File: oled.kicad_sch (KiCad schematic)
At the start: 10 parts

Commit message: wip
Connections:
- net VBUS is gone; now on net +3V3: R26.1
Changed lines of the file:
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@@
-    )
-  )
-  (symbol (lib_id "power:VBUS") (at 100.33 93.98 0) (unit 1)
-    (in_bom yes) (on_board yes) (dnp no) (fields_autoplaced)
-    (property "Reference" "#PWR02" (at 100.33 97.79 0)
-      (effects (font (size 1.27 1.27)) hide)
-    )
-    (property "Value" "VBUS" (at 100.33 90.4781 0)
-      (effects (font (size 1.27 1.27)))
-    )
-    (property "Footprint" "" (at 100.33 93.98 0)
-      (effects (font (size 1.27 1.27)) hide)
-    )
-    (property "Datasheet" "" (at 100.33 93.98 0)
-      (effects (font (size 1.27 1.27)) hide)
-    )
-    (pin "1")
-    (instances
-      (project "oled-nametag"
-        (path "/c0b8a503-1da4-4e1a-941c-dddf39a5c519"
-          (reference "#PWR02") (unit 1)
-        )
-        (path "/c0b8a503-1da4-4e1a-941c-dddf39a5c519/4a47d447-b016-4135-8945-1a7aa01f0126"
-          (reference "#PWR03") (unit 1)
-        )
-      )
     )
   )
@@
         )
       )
+    )
+  )
+  (symbol (lib_id "power:+3V3") (at 100.33 93.98 0) (unit 1)
+    (in_bom yes) (on_board yes) (dnp no) (fields_autoplaced)
+    (property "Reference" "#PWR03" (at 100.33 97.79 0)
+      (effects (font (size 1.27 1.27)) hide)
+    )
+    (property "Value" "+3V3" (at 100.33 90.4781 0)
+      (effects (font (size 1.27 1.27)))
+    )
+    (property "Footprint" "" (at 100.33 93.98 0)
+      (effects (font (size 1.27 1.27)) hide)
+    )
+    (property "Datasheet" "" (at 100.33 93.98 0)
+      (effects (font (size 1.27 1.27)) hide)
+    )
+    (pin "1")
+    (instances
+      (project "oled-nametag"
+        (path "/c0b8a503-1da4-4e1a-941c-dddf39a5c519/4a47d447-b016-4135-8945-1a7aa01f0126"
+          (reference "#PWR03") (unit 1)
+        )
+      )

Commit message: Finish first layout revision
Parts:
- added C33: 100nF, Capacitor_SMD:C_0402_1005Metric, symbol Device:C_Small
- R26: value 5.1k -> 100R; LCSC C25905 -> C25076
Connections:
- net GND: now also U1.ML (MP), C33.1
- net OLED_RST: now also C33.2
- new net GND1: U1.MR (MP)
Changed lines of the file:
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@@
 (kicad_sch (version 20230121) (generator eeschema)
   (paper "A4")
+  (junction (at 95.25 114.3) (diameter 0) (color 0 0 0 0)
+  )
   (junction (at 127 143.51) (diameter 0) (color 0 0 0 0)
   )
@@
   (junction (at 109.22 134.62) (diameter 0) (color 0 0 0 0)
   )
+  (junction (at 91.44 104.14) (diameter 0) (color 0 0 0 0)
+  )
   (junction (at 109.22 127) (diameter 0) (color 0 0 0 0)
   )
@@
     (stroke (width 0) (type default))
   )
+  (wire (pts (xy 95.25 99.06) (xy 95.25 114.3))
+    (stroke (width 0) (type default))
+  )
   (wire (pts (xy 144.78 115.57) (xy 144.78 116.84))
     (stroke (width 0) (type default))
   )
+  (wire (pts (xy 132.08 143.51) (xy 133.35 143.51))
+    (stroke (width 0) (type default))
+  )
+  (wire (pts (xy 137.16 143.51) (xy 135.89 143.51))
+    (stroke (width 0) (type default))
+  )
   (wire (pts (xy 110.49 88.9) (xy 110.49 80.01))
     (stroke (width 0) (type default))
@@
     (stroke (width 0) (type default))
   )
+  (wire (pts (xy 91.44 104.14) (xy 91.44 105.41))
+    (stroke (width 0) (type default))
+  )
   (wire (pts (xy 143.51 109.22) (xy 144.78 109.22))
     (stroke (width 0) (type default))
@@
     (stroke (width 0) (type default))
   )
+  (wire (pts (xy 135.89 142.24) (xy 135.89 143.51))
+    (stroke (width 0) (type default))
+  )
   (wire (pts (xy 129.54 87.63) (xy 132.08 87.63))
     (stroke (width 0) (type default))
@@
     (stroke (width 0) (type default))
   )
-  (wire (pts (xy 95.25 104.14) (xy 95.25 99.06))
-    (stroke (width 0) (type default))
-  )
-  (wire (pts (xy 109.22 104.14) (xy 110.49 104.14))
+  (wire (pts (xy 90.17 104.14) (xy 91.44 104.14))
     (stroke (width 0) (type default))
   )
@@
     (stroke (width 0) (type default))
   )
+  (wire (pts (xy 91.44 110.49) (xy 91.44 111.76))
+    (stroke (width 0) (type default))
+  )
+  (wire (pts (xy 132.08 144.78) (xy 132.08 143.51))
+    (stroke (width 0) (type default))
+  )
   (wire (pts (xy 109.22 132.08) (xy 109.22 129.54))
     (stroke (width 0) (type default))
   )
+  (wire (pts (xy 133.35 142.24) (xy 133.35 143.51))
+    (stroke (width 0) (type default))
+  )
   (wire (pts (xy 109.22 129.54) (xy 109.22 127))
     (stroke (width 0) (type default))
   )
+  (wire (pts (xy 91.44 104.14) (xy 110.49 104.14))
+    (stroke (width 0) (type default))
+  )
   (wire (pts (xy 172.72 96.52) (xy 143.51 96.52))
     (stroke (width 0) (type default))
@@
   )
   (wire (pts (xy 144.78 109.22) (xy 144.78 110.49))
+    (stroke (width 0) (type default))
+  )
+  (wire (pts (xy 137.16 144.78) (xy 137.16 143.51))
     (stroke (width 0) (type default))
   )
@@
     (effects (font (size 1.27 1.27)) (justify left))
   )
-  (hierarchical_label "OLED_RST" (shape input) (at 109.22 104.14 180) (fields_autoplaced)
+  (hierarchical_label "OLED_RST" (shape input) (at 90.17 104.14 180) (fields_autoplaced)
     (effects (font (size 1.27 1.27)) (justify right))
   )
@@
   )
   (symbol (lib_id "OLED:OLED_256x64") (at 127 116.84 0) (unit 1)
-    (in_bom yes) (on_board yes) (dnp no) (fields_autoplaced)
-    (property "Reference" "U1" (at 130.2259 141.2955 0)
+    (in_bom yes) (on_board yes) (dnp no)
+    (property "Reference" "U1" (at 118.11 92.71 0)
       (effects (font (size 1.27 1.27)) (justify left))
     )
@@
     (pin "29")
     (pin "30")
+    (pin "ML")
+    (pin "MR")
     (instances
       (project "oled-nametag"
@@
         (path "/c0b8a503-1da4-4e1a-941c-dddf39a5c519/4a47d447-b016-4135-8945-1a7aa01f0126"
           (reference "U1") (unit 1)
+        )
+      )
+    )
+  )
+  (symbol (lib_id "power:GND") (at 91.44 111.76 0) (unit 1)
+    (in_bom yes) (on_board yes) (dnp no) (fields_autoplaced)
+    (property "Reference" "#PWR01" (at 91.44 118.11 0)
+      (effects (font (size 1.27 1.27)) hide)
+    )
+    (property "Value" "GND" (at 91.44 115.8955 0)
+      (effects (font (size 1.27 1.27)))
+    )
+    (property "Footprint" "" (at 91.44 111.76 0)
+      (effects (font (size 1.27 1.27)) hide)
+    )
+    (property "Datasheet" "" (at 91.44 111.76 0)
+      (effects (font (size 1.27 1.27)) hide)
+    )
+    (pin "1")
+    (instances
+      (project "oled-nametag"
+        (path "/c0b8a503-1da4-4e1a-941c-dddf39a5c519/4a47d447-b016-4135-8945-1a7aa01f0126"
+          (reference "#PWR01") (unit 1)
         )
       )
@@
     )
   )
+  (symbol (lib_id "power:GND1") (at 137.16 144.78 0) (unit 1)
+    (in_bom yes) (on_board yes) (dnp no) (fields_autoplaced)
+    (property "Reference" "#PWR082" (at 137.16 151.13 0)
+      (effects (font (size 1.27 1.27)) hide)
+    )
+    (property "Value" "GND1" (at 137.16 148.9155 0)
+      (effects (font (size 1.27 1.27)))
+    )
+    (property "Footprint" "" (at 137.16 144.78 0)
+      (effects (font (size 1.27 1.27)) hide)
+    )
+    (property "Datasheet" "" (at 137.16 144.78 0)
+      (effects (font (size 1.27 1.27)) hide)
+    )
+    (pin "1")
+    (instances
+      (project "oled-nametag"
+        (path "/c0b8a503-1da4-4e1a-941c-dddf39a5c519/4a47d447-b016-4135-8945-1a7aa01f0126"
+          (reference "#PWR082") (unit 1)
+        )
+      )
+    )
+  )
   (symbol (lib_id "power:GND") (at 144.78 116.84 0) (unit 1)
     (in_bom yes) (on_board yes) (dnp no) (fields_autoplaced)
@@
       (effects (font (size 1.27 1.27)))
     )
-    (property "Value" "5.1k" (at 107.95 93.98 90)
+    (property "Value" "100R" (at 107.95 93.98 90)
       (effects (font (size 1.27 1.27)))
     )
@@
       (effects (font (size 1.27 1.27)) hide)
     )
-    (property "LCSC" "C25905" (at 106.68 96.52 0)
+    (property "LCSC" "C25076" (at 106.68 96.52 0)
       (effects (font (size 1.27 1.27)) hide)
     )
@@
         (path "/c0b8a503-1da4-4e1a-941c-dddf39a5c519/4a47d447-b016-4135-8945-1a7aa01f0126"
           (reference "#PWR017") (unit 1)
-        )
-      )
-    )
-  )
-  (symbol (lib_id "power:GND") (at 95.25 104.14 0) (unit 1)
-    (in_bom yes) (on_board yes) (dnp no) (fields_autoplaced)
-    (property "Reference" "#PWR01" (at 95.25 110.49 0)
-      (effects (font (size 1.27 1.27)) hide)
-    )
-    (property "Value" "GND" (at 95.25 108.2755 0)
-      (effects (font (size 1.27 1.27)))
-    )
-    (property "Footprint" "" (at 95.25 104.14 0)
-      (effects (font (size 1.27 1.27)) hide)
-    )
-    (property "Datasheet" "" (at 95.25 104.14 0)
-      (effects (font (size 1.27 1.27)) hide)
-    )
-    (pin "1")
-    (instances
-      (project "oled-nametag"
-        (path "/c0b8a503-1da4-4e1a-941c-dddf39a5c519"
-          (reference "#PWR01") (unit 1)
-        )
-        (path "/c0b8a503-1da4-4e1a-941c-dddf39a5c519/4a47d447-b016-4135-8945-1a7aa01f0126"
-          (reference "#PWR01") (unit 1)
         )
       )
@@
         )
       )
+    )
+  )
+  (symbol (lib_id "power:GND") (at 132.08 144.78 0) (unit 1)
+    (in_bom yes) (on_board yes) (dnp no) (fields_autoplaced)
+    (property "Reference" "#PWR014" (at 132.08 151.13 0)
+      (effects (font (size 1.27 1.27)) hide)
+    )
+    (property "Value" "GND" (at 132.08 148.9155 0)
+      (effects (font (size 1.27 1.27)))
+    )
+    (property "Footprint" "" (at 132.08 144.78 0)
+      (effects (font (size 1.27 1.27)) hide)
+    )
+    (property "Datasheet" "" (at 132.08 144.78 0)
+      (effects (font (size 1.27 1.27)) hide)
+    )
+    (pin "1")
+    (instances
+      (project "oled-nametag"
+        (path "/c0b8a503-1da4-4e1a-941c-dddf39a5c519"
+          (reference "#PWR014") (unit 1)
+        )
+        (path "/c0b8a503-1da4-4e1a-941c-dddf39a5c519/4a47d447-b016-4135-8945-1a7aa01f0126"
+          (reference "#PWR081") (unit 1)
+        )
+      )
+    )
+  )
+  (symbol (lib_id "Device:C_Small") (at 91.44 107.95 0) (mirror x) (unit 1)
+    (in_bom yes) (on_board yes) (dnp no)
+    (property "Reference" "C33" (at 87.63 109.22 0)
+      (effects (font (size 1.27 1.27)))
+    )
+    (property "Value" "100nF" (at 86.36 106.68 0)
+      (effects (font (size 1.27 1.27)))
+    )
+    (property "Footprint" "Capacitor_SMD:C_0402_1005Metric" (at 91.44 107.95 0)
+      (effects (font (size 1.27 1.27)) hide)
+    )
+    (property "Datasheet" "~" (at 91.44 107.95 0)
+      (effects (font (size 1.27 1.27)) hide)
+    )
+    (property "LCSC" "C1525" (at 91.44 107.95 90)
+      (effects (font (size 1.27 1.27)) hide)
+    )
+    (pin "1")
+    (pin "2")
+    (instances
+      (project "rgb-led-nametag-48x16"
+        (path "/751d823e-1d7b-4501-9658-d06d459b0e16"
+          (reference "C33") (unit 1)
+        )
+      )
+      (project "oled-nametag"
+        (path "/c0b8a503-1da4-4e1a-941c-dddf39a5c519"
+          (reference "C16") (unit 1)
+        )
+        (path "/c0b8a503-1da4-4e1a-941c-dddf39a5c519/2d7ad3ad-5e88-44f5-86dc-1521acbc3a27"
+          (reference "C17") (unit 1)
+        )
+        (path "/c0b8a503-1da4-4e1a-941c-dddf39a5c519/4a47d447-b016-4135-8945-1a7aa01f0126"
+          (reference "C39") (unit 1)
+        )
+      )

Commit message: Start rev1.1
Fixed bugs:
 - Swapped D+ and D-
 - Insufficient pull-down strength on VBUS
 - Default OLED to 4-wire SPI
 - Swap VBUS detect divider from 2/3 to 1/3
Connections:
- net +3V3: no longer R26.1
- net GND: now also R26.1
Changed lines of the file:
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@@
   (junction (at 124.46 88.9) (diameter 0) (color 0 0 0 0)
   )
+  (junction (at 95.25 99.06) (diameter 0) (color 0 0 0 0)
+  )
   (junction (at 109.22 134.62) (diameter 0) (color 0 0 0 0)
   )
@@
     (stroke (width 0) (type default))
   )
+  (wire (pts (xy 95.25 96.52) (xy 104.14 96.52))
+    (stroke (width 0) (type default))
+  )
   (wire (pts (xy 109.22 109.22) (xy 110.49 109.22))
     (stroke (width 0) (type default))
@@
     (stroke (width 0) (type default))
   )
-  (wire (pts (xy 100.33 96.52) (xy 104.14 96.52))
-    (stroke (width 0) (type default))
-  )
   (wire (pts (xy 109.22 139.7) (xy 109.22 137.16))
     (stroke (width 0) (type default))
@@
     (stroke (width 0) (type default))
   )
-  (wire (pts (xy 100.33 93.98) (xy 100.33 96.52))
-    (stroke (width 0) (type default))
-  )
   (wire (pts (xy 109.22 129.54) (xy 110.49 129.54))
     (stroke (width 0) (type default))
@@
   )
   (wire (pts (xy 129.54 78.74) (xy 129.54 87.63))
+    (stroke (width 0) (type default))
+  )
+  (wire (pts (xy 95.25 96.52) (xy 95.25 99.06))
     (stroke (width 0) (type default))
   )
@@
         )
       )
-    )
-  )
-  (symbol (lib_id "power:+3V3") (at 100.33 93.98 0) (unit 1)
-    (in_bom yes) (on_board yes) (dnp no) (fields_autoplaced)
-    (property "Reference" "#PWR03" (at 100.33 97.79 0)
-      (effects (font (size 1.27 1.27)) hide)
-    )
-    (property "Value" "+3V3" (at 100.33 90.4781 0)
-      (effects (font (size 1.27 1.27)))
-    )
-    (property "Footprint" "" (at 100.33 93.98 0)
-      (effects (font (size 1.27 1.27)) hide)
-    )
-    (property "Datasheet" "" (at 100.33 93.98 0)
-      (effects (font (size 1.27 1.27)) hide)
-    )
-    (pin "1")
-    (instances
-      (project "oled-nametag"
-        (path "/c0b8a503-1da4-4e1a-941c-dddf39a5c519/4a47d447-b016-4135-8945-1a7aa01f0126"
-          (reference "#PWR03") (unit 1)
-        )
-      )

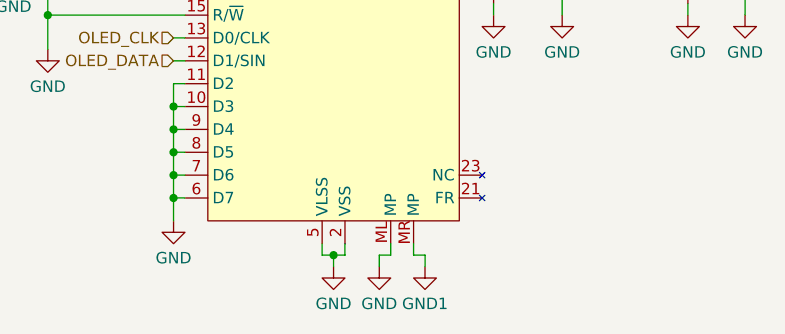
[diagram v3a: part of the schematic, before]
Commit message: Do rough component placement
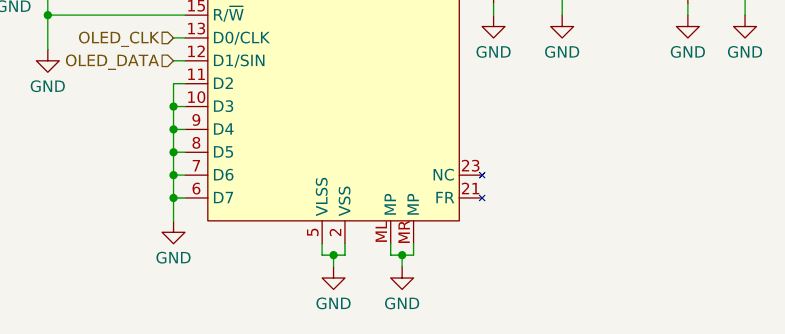
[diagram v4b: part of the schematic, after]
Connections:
- net GND1 is gone; now on net GND: U1.MR (MP)

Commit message: Finsh first layout iteration
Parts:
- added C6: 10uF 25V, Capacitor_SMD:C_0603_1608Metric, symbol Device:C_Small
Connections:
- net GND: now also C6.2
- net VCC: now also C6.1
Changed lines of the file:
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@@
   (junction (at 127 143.51) (diameter 0) (color 0 0 0 0)
   )
+  (junction (at 139.7 87.63) (diameter 0) (color 0 0 0 0)
+  )
   (junction (at 95.25 116.84) (diameter 0) (color 0 0 0 0)
   )
@@
   (junction (at 134.62 143.51) (diameter 0) (color 0 0 0 0)
   )
+  (junction (at 129.54 80.01) (diameter 0) (color 0 0 0 0)
+  )
   (junction (at 109.22 129.54) (diameter 0) (color 0 0 0 0)
   )
@@
     (stroke (width 0) (type default))
   )
+  (wire (pts (xy 129.54 80.01) (xy 129.54 87.63))
+    (stroke (width 0) (type default))
+  )
   (wire (pts (xy 129.54 87.63) (xy 132.08 87.63))
     (stroke (width 0) (type default))
@@
     (stroke (width 0) (type default))
   )
+  (wire (pts (xy 139.7 80.01) (xy 139.7 87.63))
+    (stroke (width 0) (type default))
+  )
   (wire (pts (xy 109.22 139.7) (xy 109.22 137.16))
     (stroke (width 0) (type default))
   )
+  (wire (pts (xy 129.54 76.2) (xy 129.54 80.01))
+    (stroke (width 0) (type default))
+  )
   (wire (pts (xy 90.17 104.14) (xy 91.44 104.14))
     (stroke (width 0) (type default))
@@
     (stroke (width 0) (type default))
   )
+  (wire (pts (xy 137.16 80.01) (xy 139.7 80.01))
+    (stroke (width 0) (type default))
+  )
   (wire (pts (xy 127 143.51) (xy 128.27 143.51))
     (stroke (width 0) (type default))
@@
     (stroke (width 0) (type default))
   )
+  (wire (pts (xy 129.54 80.01) (xy 132.08 80.01))
+    (stroke (width 0) (type default))
+  )
   (wire (pts (xy 129.54 87.63) (xy 129.54 91.44))
-    (stroke (width 0) (type default))
-  )
-  (wire (pts (xy 129.54 78.74) (xy 129.54 87.63))
     (stroke (width 0) (type default))
   )
@@
     (effects (font (size 1.27 1.27)) (justify right))
   )
-  (hierarchical_label "VCC_OLED" (shape input) (at 129.54 78.74 90) (fields_autoplaced)
+  (hierarchical_label "VCC_OLED" (shape input) (at 129.54 76.2 90) (fields_autoplaced)
     (effects (font (size 1.27 1.27)) (justify left))
   )
@@
         )
       )
+    )
+  )
+  (symbol (lib_id "Device:C_Small") (at 134.62 80.01 90) (unit 1)
+    (in_bom yes) (on_board yes) (dnp no) (fields_autoplaced)
+    (property "Reference" "C6" (at 134.6263 75.438 90)
+      (effects (font (size 1.27 1.27)))
+    )
+    (property "Value" "10uF 25V" (at 134.6263 77.359 90)
+      (effects (font (size 1.27 1.27)))
+    )
+    (property "Footprint" "Capacitor_SMD:C_0603_1608Metric" (at 134.62 80.01 0)
+      (effects (font (size 1.27 1.27)) hide)
+    )
+    (property "Datasheet" "~" (at 134.62 80.01 0)
+      (effects (font (size 1.27 1.27)) hide)
+    )
+    (property "LCSC" "C96446" (at 134.62 80.01 0)
+      (effects (font (size 1.27 1.27)) hide)
+    )
+    (pin "1")
+    (pin "2")
+    (instances
+      (project "oled-nametag"
+        (path "/c0b8a503-1da4-4e1a-941c-dddf39a5c519"
+          (reference "C6") (unit 1)
+        )
+        (path "/c0b8a503-1da4-4e1a-941c-dddf39a5c519/4a47d447-b016-4135-8945-1a7aa01f0126"
+          (reference "C43") (unit 1)
+        )
+      )
